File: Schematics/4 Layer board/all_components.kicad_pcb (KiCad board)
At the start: 4 copper layers, 91.8 x 93.6 mm, 80 parts, among them J2 Conn_01x01, J3 5V-Relay, J4 5V-Relay, J5 S8B-PHDSS, J9 3-pin-header, Q1 OPTOCOUPLER, Q2 OPTOCOUPLER, T1 PNP, T2 PNP, T3 PNP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

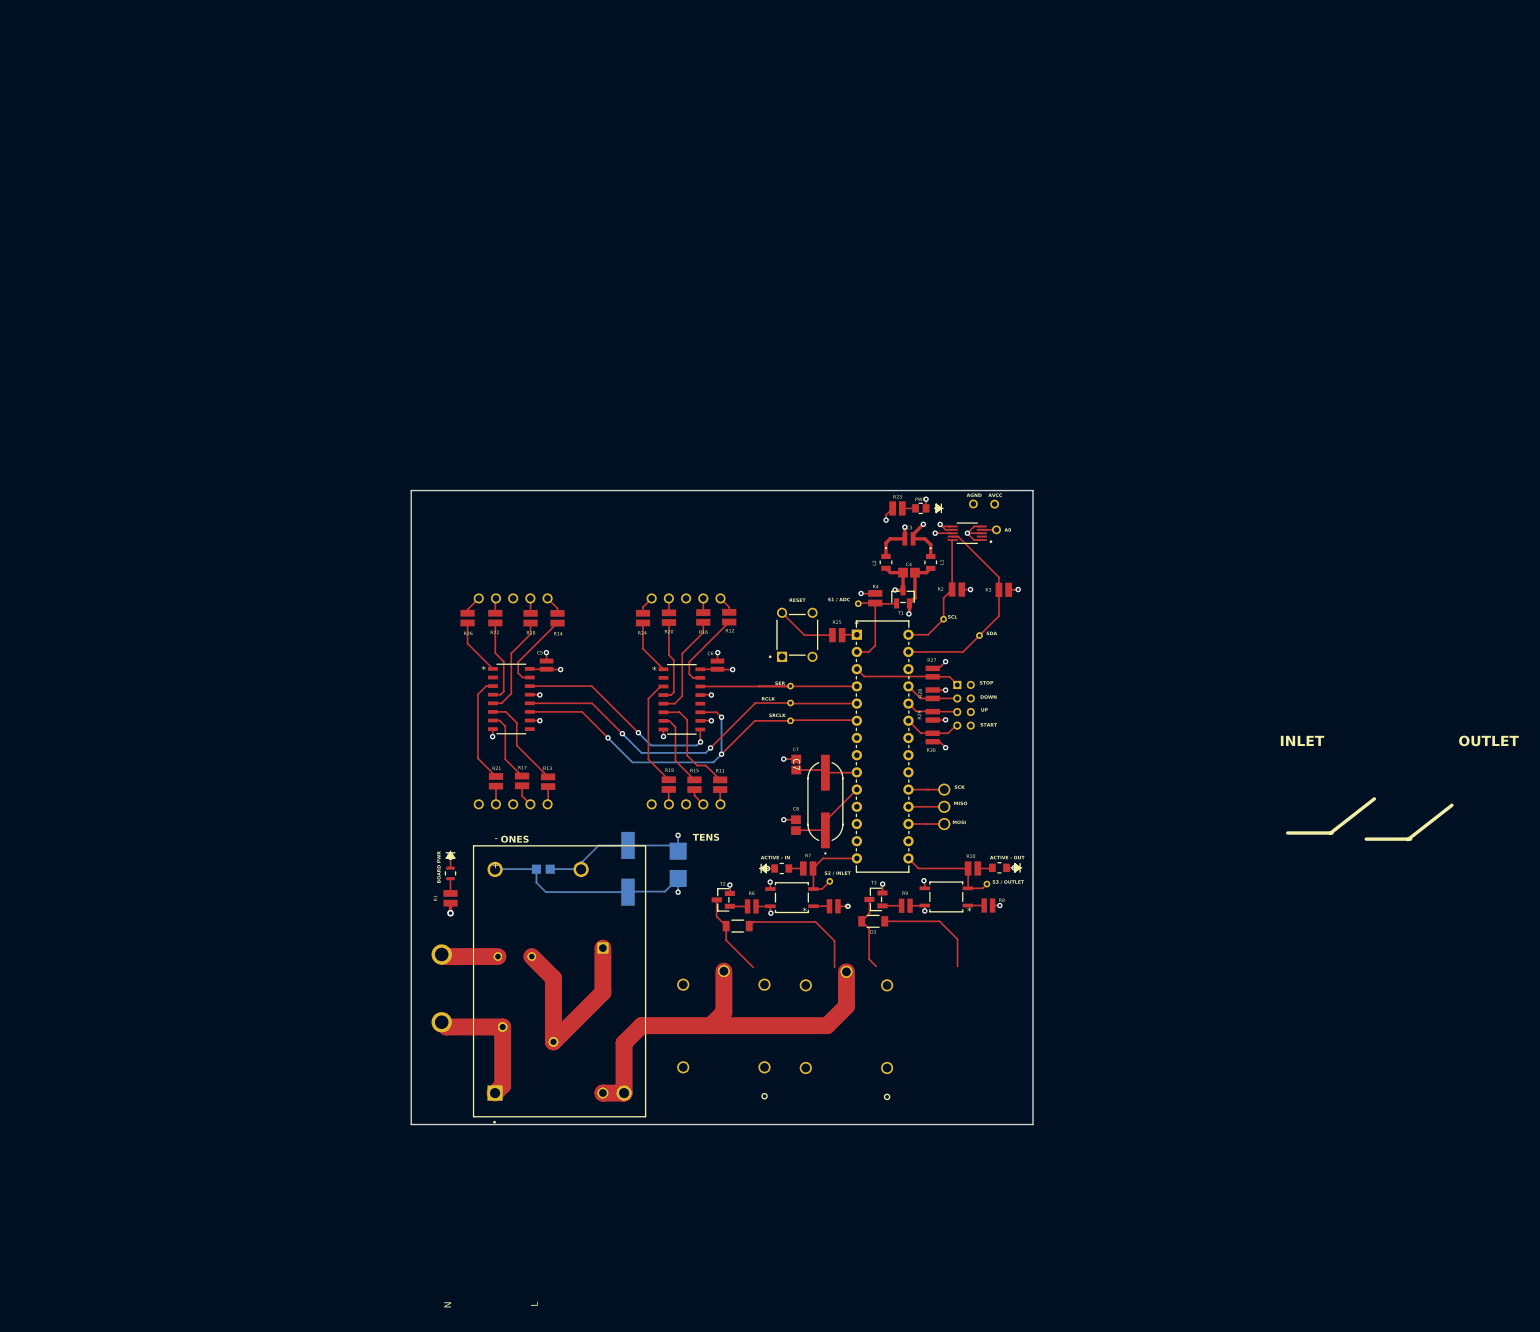
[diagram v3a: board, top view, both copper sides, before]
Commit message: more CAD files and updated layout
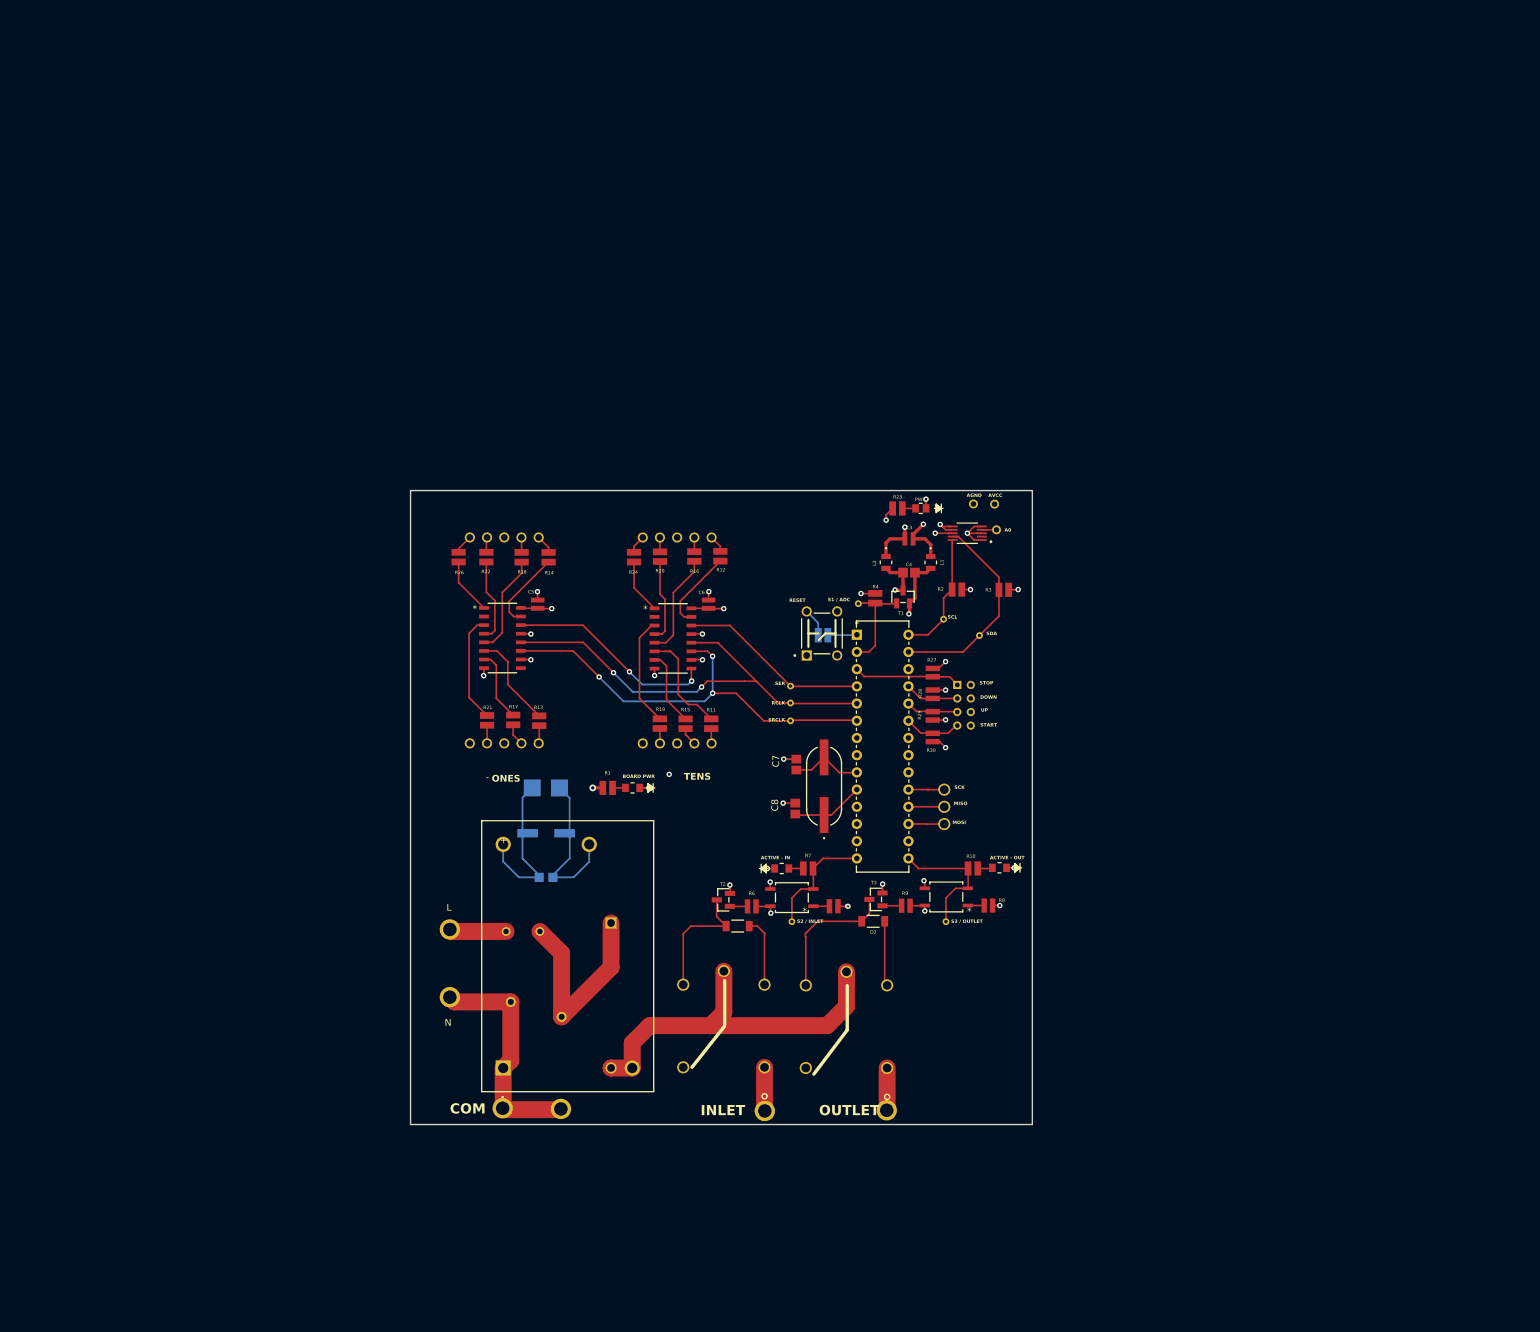
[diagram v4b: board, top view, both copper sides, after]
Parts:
- added S4: Conn_01x01, pPSI:1 pin header, F.Cu at (111.0, 162.2)
- added S5: Conn_01x01, pPSI:1 pin header, F.Cu at (129.0, 162.1)
- added S6: Conn_01x01, pPSI:1 pin header, F.Cu at (80.9, 161.9)
- added S7: Conn_01x01, pPSI:1 pin header, F.Cu at (72.3, 161.8)
- C2: footprint pPSI:220uF electrolytic capacitor -> pPSI:220uF Cap (e)
- C7: footprint pPSI:22pFCeramicCap -> pPSI:22pF Cap (c)
- C8: value C0805C220J5GAC7210 -> ~; footprint pPSI:22pFCeramicCap -> pPSI:22pF Cap (c)
- LED1: footprint pPSI:green LED -> pPSI:red LED
- R25: moved to B.Cu
- moved LED1 29.7 mm to (91.5, 114.5), turned to 180 degrees
- moved R1 28.4 mm to (87.8, 114.5), turned to 180 degrees
- moved TVS1 22.6 mm to (78.6, 114.5), turned to 180 degrees
- moved C2 13.2 mm to (78.7, 121.2), turned to 180 degrees
- moved C5 9.10 mm to (77.5, 87.4)
- moved ONES-SR1 9.10 mm to (72.3, 92.4)
- moved ONES1 9.10 mm to (89.3, 89.1)
- moved R15 9.10 mm to (99.3, 105.0)
- moved R26 9.10 mm to (65.8, 80.4)
- moved TENS-SR1 9.10 mm to (97.4, 92.4)
- moved C6 9.10 mm to (102.7, 87.4)
- moved R11 9.10 mm to (103.1, 105.0)
- moved R12 9.10 mm to (104.4, 80.3)
- moved R13 9.10 mm to (77.7, 104.6)
- moved R14 9.10 mm to (79.1, 80.5)
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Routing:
- net /GND: track 94.4 -> 72.4 mm, vias 18 -> 17
- net /Neutral: track 19.5 -> 34.2 mm
- net /RCLK: track 54.5 -> 66.9 mm
- net Net-(D2-Pad2): track 11.3 -> 20.4 mm
- net Net-(D1-Pad2): track 12.2 -> 18.8 mm
- net /N/O_INLET: track 0.00 -> 6.46 mm
- net /N/O_OUTLET: track 0.00 -> 6.27 mm
- net /LIVE: track 68.1 -> 63.3 mm
- net Net-(B1-Pad2): track 8.81 -> 4.20 mm
- net /S2: track 13.0 -> 17.4 mm
- net /S3: track 15.5 -> 19.7 mm
- net Net-(11-PCINT14/RESETPC6): track 2.20 -> 4.30 mm
- net /VCC: track 65.6 -> 67.2 mm
- net /OSC1: track 9.13 -> 10.7 mm
- net /OSC2: track 12.3 -> 10.8 mm
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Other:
- board text added: "COM"
- board text removed: "CAUTION"

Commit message: updated cad files
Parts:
- removed AGND1, AVCC1, S4, S5, S6, S7: Conn_01x01, pPSI:1 pin header
- added J6: OSTVN03A150, pPSI:1x3 terminal block, F.Cu at (149.2, 72.7)
- added J7: OSTTF020161, pPSI:1x2 terminal block, F.Cu at (114.0, 164.4)
- J1: value ~ -> OSTTF020161; footprint pPSI:2 pin header -> pPSI:1x2 terminal block; moved to F.Cu
- J2: value Conn_01x01 -> OSTTF020161; footprint pPSI:1 pin header -> pPSI:1x2 terminal block
- J5: moved to F.Cu
- moved J2 113.1 mm to (74.2, 164.4), turned to 180 degrees
- moved J5 5.95 mm to (139.4, 105.2), turned to 90 degrees
- moved J1 5.49 mm to (63.2, 140.8), turned to 90 degrees
- moved A3 4.58 mm to (141.2, 125.0)
- moved R10 4.28 mm to (137.5, 125.8), turned to -90 degrees
- moved LED1 3.00 mm to (91.5, 117.5)
- moved R1 3.00 mm to (87.8, 117.5)
- moved C5 2.92 mm to (80.3, 86.8)
- moved ONES-SR1 2.92 mm to (75.1, 91.8)
- moved ONES1 2.92 mm to (92.2, 88.6)
- moved R12 2.92 mm to (107.3, 79.7)
- moved R13 2.92 mm to (80.6, 104.0)
- moved R14 2.92 mm to (81.9, 79.9)
- moved R15 2.92 mm to (102.2, 104.5)
- moved R19 2.92 mm to (98.4, 104.4)
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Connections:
- J1 pad 1: /LIVE -> /Neutral
- J1 pad 2: /Neutral -> /LIVE
- J2 pad 1: /A0 -> /Neutral
- J5 pad 1: /STOP -> /START
- J5 pad 3: /DOWN -> /UP
- J5 pad 5: /UP -> /DOWN
- J5 pad 7: /START -> /STOP
- R27 pad 2: /STOP -> /START
- R28 pad 2: /DOWN -> /UP
- R29 pad 2: /UP -> /DOWN
- R30 pad 2: /START -> /STOP
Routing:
- net /N/O_OUTLET: track 6.27 -> 20.3 mm
- net /AGND: track 19.0 -> 27.1 mm
- net /A0: track 2.17 -> 6.69 mm
- net /RCLK: track 66.9 -> 63.5 mm
- net Net-(D1-Pad2): track 18.8 -> 15.8 mm
- net /SRCLK: track 63.9 -> 61.2 mm
- net /N/O_INLET: track 6.46 -> 8.89 mm
- net /LIVE: track 63.3 -> 65.4 mm
- net /S3: track 19.7 -> 18.0 mm
- net /GND: track 72.4 -> 74.1 mm
- net /AVCC: track 12.0 -> 10.4 mm
- net /VCC: track 67.2 -> 65.6 mm, vias 17 -> 16
- net /SER: track 28.2 -> 27.0 mm
- net /T10: track 15.6 -> 14.8 mm
- net Net-(A3-Pad2): track 2.20 -> 2.72 mm
- removed copper zone on In1.Cu, net /AGND
- removed copper zone on In2.Cu, net /AVCC
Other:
- board size 91.8 x 93.6 mm -> 95.3 x 99.2 mm
